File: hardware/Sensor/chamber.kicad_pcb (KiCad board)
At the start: 2 copper layers, 100 x 100 mm, 96 parts, among them J1 USB_B_Micro, J32 RF_Shield_Two_Pieces, J33 RF_Shield_Two_Pieces, J34 Conn_Coaxial, J51 Conn_02x05_Counter_Clockwise, J52 Conn_01x04, Q31 BC859, Q32 Q_NMOS_GDS, Q51 2N7002, Q52 Q_NPN_BEC, SW31 SW_DPDT_x2, SW32 SW_DPDT_x2, U31 MC34063AD, U32 LMC662, U33 LM358, U51 Opamp_Dual_Generic, U52 MCP3425A0T-ECH, U53 MCP3425A0T-ECH, U54 STM8S003F3P

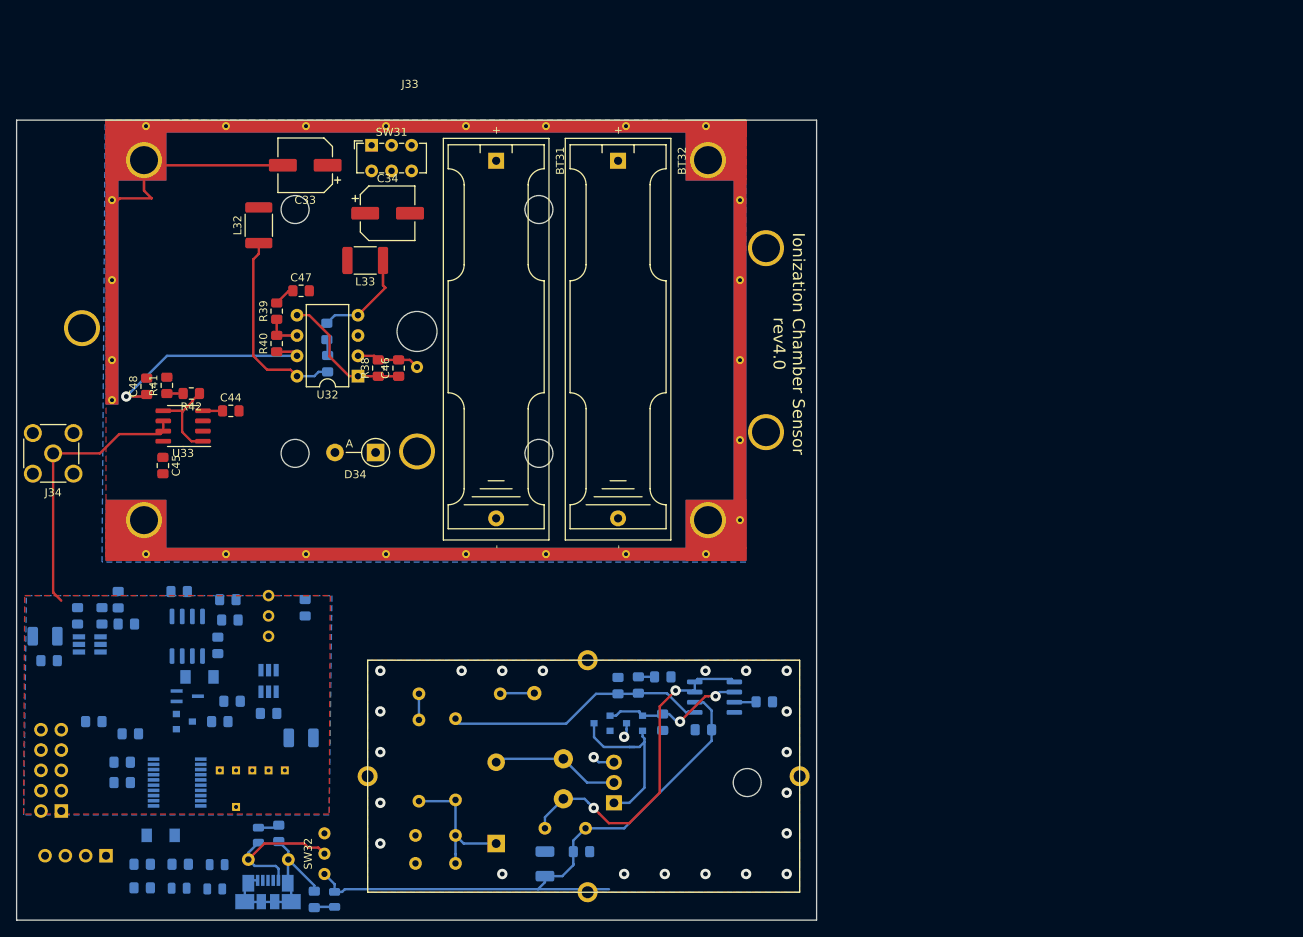
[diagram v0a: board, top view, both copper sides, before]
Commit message: ground between masses
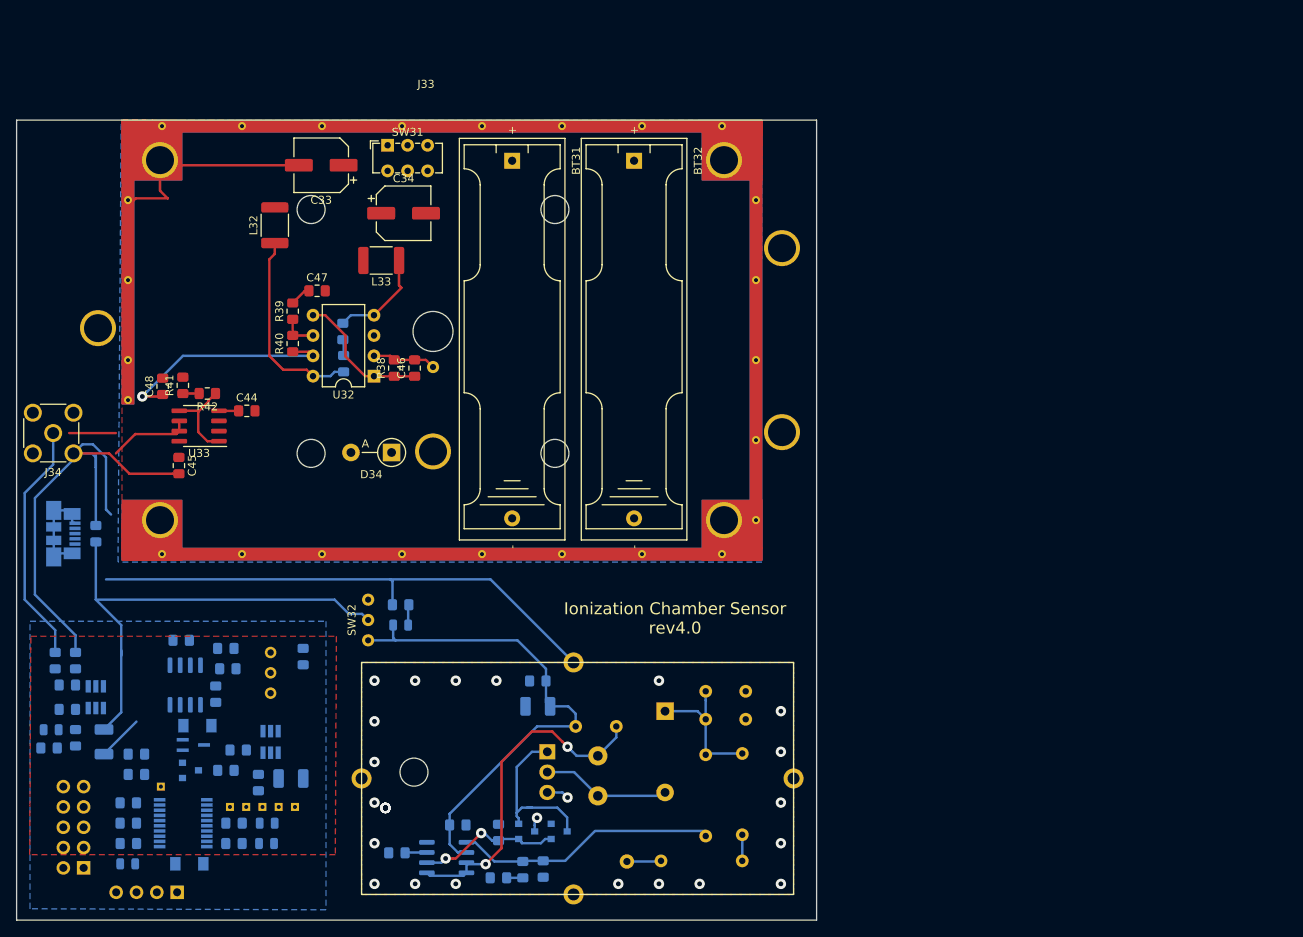
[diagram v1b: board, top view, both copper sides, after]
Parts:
- C1: footprint Capacitor_THT:C_Disc_D4.3mm_W1.9mm_P5.00mm -> Capacitor_SMD:C_0805_2012Metric_Pad1.15x1.40mm_HandSolder
- moved J32 61.8 mm to (95.4, 122.1), turned to 0 degrees
- moved J1 51.6 mm to (58.2, 106.0), turned to 90 degrees
- moved C32 49.7 mm to (99.9, 145.9), turned to 180 degrees
- moved C1 47.3 mm to (62.2, 106.1), turned to 270 degrees
- moved R36 42.9 mm to (143.0, 143.7), turned to 90 degrees
- moved U31 39.0 mm to (106.1, 146.5), turned to 0 degrees
- moved R43 38.4 mm to (100.3, 114.9), turned to 180 degrees
- moved C41 38.0 mm to (138.5, 125.8), turned to 0 degrees
- moved D31 35.3 mm to (100.3, 117.5), turned to 180 degrees
- moved C43 34.5 mm to (138.5, 129.3), turned to 0 degrees
- moved C31 32.9 mm to (107.5, 142.5), turned to 180 degrees
- moved R35 32.4 mm to (112.6, 149.1), turned to 180 degrees
- moved R33 31.8 mm to (138.5, 133.7), turned to 270 degrees
- moved R1 30.6 mm to (56.4, 132.8), turned to 0 degrees
- moved SW32 29.7 mm to (93.7, 116.8)
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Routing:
- net GND: track 57.9 -> 187.7 mm, vias 23 -> 28
- net VCC_5V: track 19.2 -> 61.4 mm
- net Net-(C2-Pad1): track 75.2 -> 62.4 mm
- net analog_output: track 35.0 -> 46.7 mm
- net Net-(D1-Pad1): track 2.67 -> 0.00 mm
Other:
- board text added: "400V DC chamber polarization"
- board text added: "Chamber signal amplifier"
- board text added: "DAC converter"

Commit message: befor board flip
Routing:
- net GND: track 187.7 -> 191.8 mm, vias 28 -> 20
- net Net-(C2-Pad1): track 62.4 -> 61.7 mm
- net Net-(C39-Pad1): track 32.5 -> 33.0 mm
- net analog_output: track 46.7 -> 46.1 mm

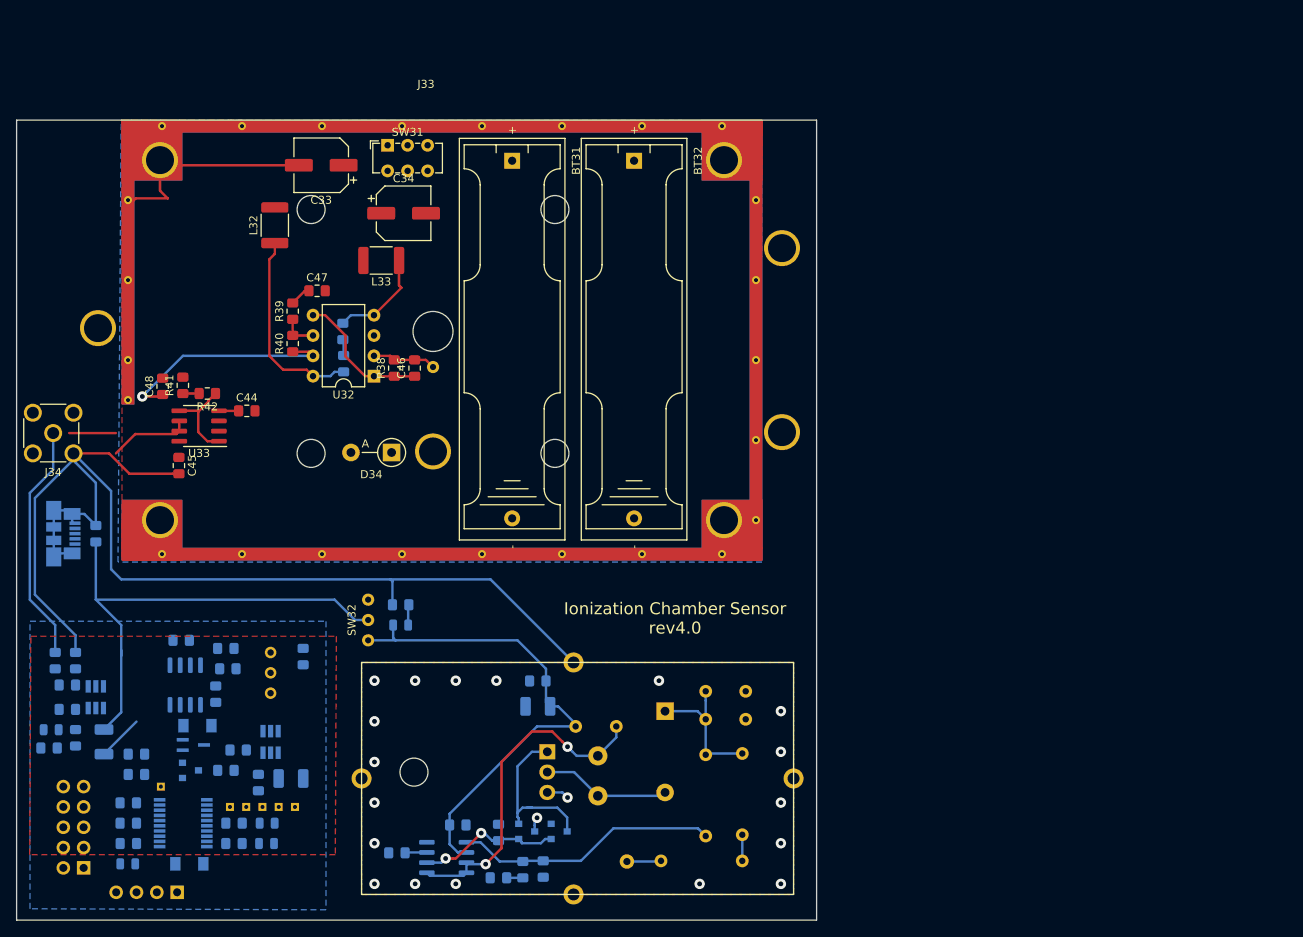
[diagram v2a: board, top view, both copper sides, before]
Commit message: dirty version of adc routing
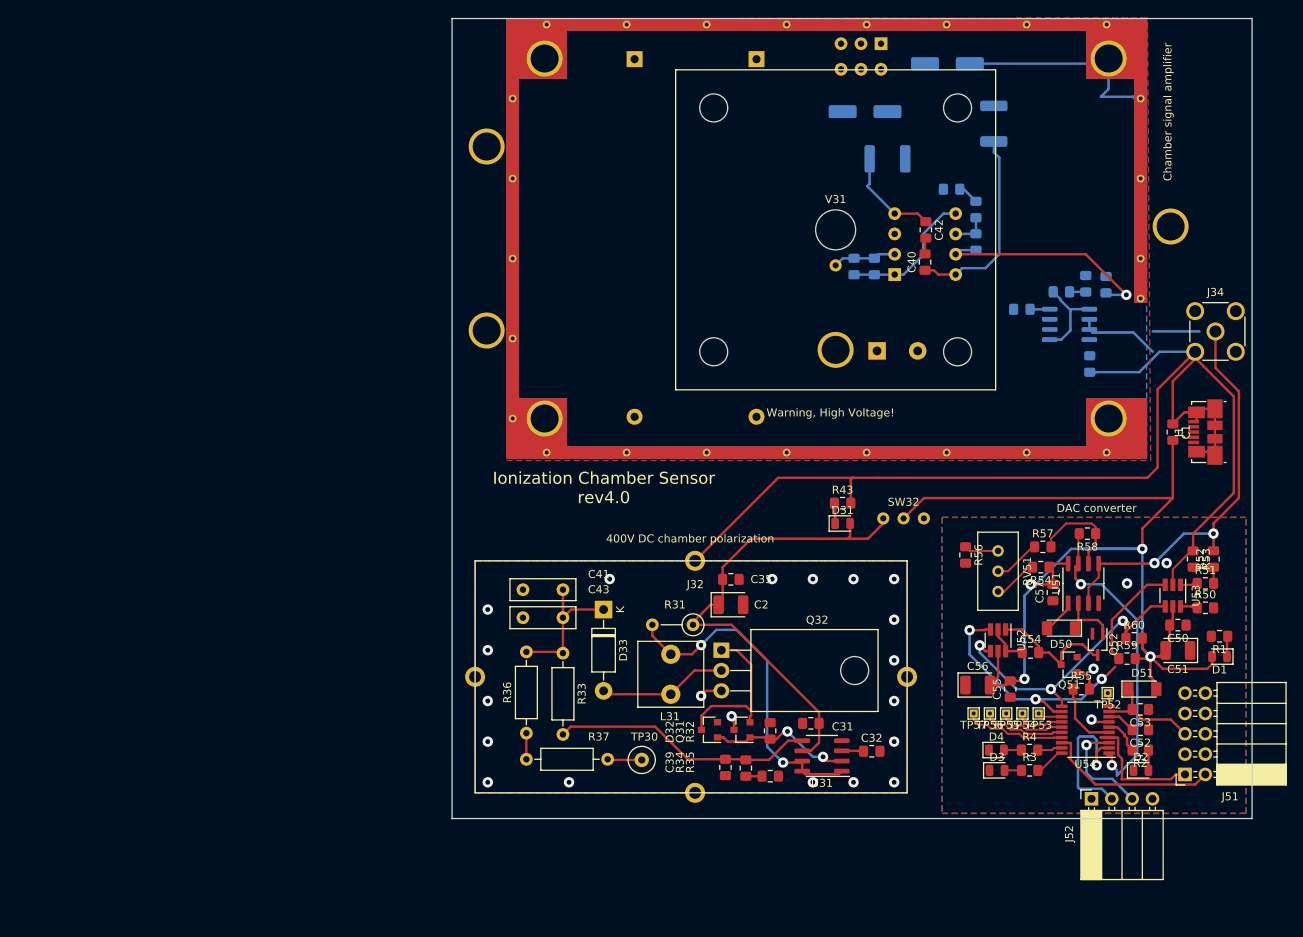
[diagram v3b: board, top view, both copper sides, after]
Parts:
- BT31, BT32, C33, C34, C44, C45, C46, C47, C48, D34, J33, L32, L33, R38, R39, R40, R41, R42, SW31, U32, U33: moved to B.Cu
- C1, C2, C31, C32, C35, C39, C40, C41, C42, C43, C50, C51, C52, C53, C54, C55, C56, C57, D1, D2, D3, D31, D32, D33, D4, D50, D51, J1, J32, J51, J52, L31, Q31, Q32, Q51, Q52, R1, R2, R3, R31, R32, R33, R34, R35, R36, R37, R4, R43, R50, R51, R52, R53, R54, R55, R56, R57, R58, R59, R60, RV51, TP30, TP52, TP53, TP54, TP55, TP56, TP57, U31, U51, U52, U53, U54, V31: moved to F.Cu
- moved R1 147.0 mm to (202.7, 118.9), turned to 180 degrees
- moved D1 146.3 mm to (202.7, 121.4), turned to 180 degrees
- moved J34 145.8 mm to (202.2, 80.8), turned to 270 degrees
- moved R52 145.3 mm to (201.9, 109.2)
- moved J1 143.3 mm to (200.9, 93.3)
- moved R50 142.8 mm to (200.9, 115.3), turned to 0 degrees
- moved R51 142.8 mm to (200.9, 112.3), turned to 0 degrees
- moved R53 140.3 mm to (199.4, 109.2)
- moved C50 138.5 mm to (197.5, 117.5), turned to 180 degrees
- moved J51 138.2 mm to (198.4, 136.1), turned to 180 degrees
- moved C1 135.2 mm to (196.8, 93.4)
- moved U53 135.2 mm to (196.8, 113.8)
- moved C51 134.7 mm to (197.5, 120.7), turned to 180 degrees
- moved J33 128.7 mm to (193.6, 41.7), turned to 180 degrees
- moved D2 127.2 mm to (192.9, 135.6), turned to 0 degrees
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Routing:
- net VCC_5V: track 61.4 -> 143.0 mm, vias 0 -> 4
- net /DataAcquisition/SCL: track 0.00 -> 45.9 mm, vias 0 -> 3
- net /DataAcquisition/INT0: track 0.00 -> 40.0 mm, vias 0 -> 2
- net /DataAcquisition/SDA: track 0.00 -> 38.0 mm, vias 0 -> 3
- net /DataAcquisition/SWIM: track 0.00 -> 22.1 mm
- net analog_output: track 46.1 -> 67.5 mm, vias 0 -> 2
- net /DataAcquisition/TX: track 0.00 -> 20.1 mm, vias 0 -> 1
- net /DataAcquisition/RST: track 0.00 -> 16.7 mm
- net Net-(C54-Pad2): track 0.00 -> 15.8 mm
- net /DataAcquisition/VCC_PROG: track 0.00 -> 13.6 mm
- net /DataAcquisition/RX: track 0.00 -> 13.5 mm, vias 0 -> 1
- net Net-(TP57-Pad1): track 0.00 -> 12.7 mm
- net Net-(R57-Pad2): track 0.00 -> 12.5 mm
- net Net-(TP56-Pad1): track 0.00 -> 10.6 mm
- net /DataAcquisition/RST_PEAK: track 0.00 -> 8.73 mm
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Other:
- net class Default: clearance 0.3048 -> 0.254
- rule trace_clearance: 0.3048 -> 0.254

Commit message: ruting amplifier part
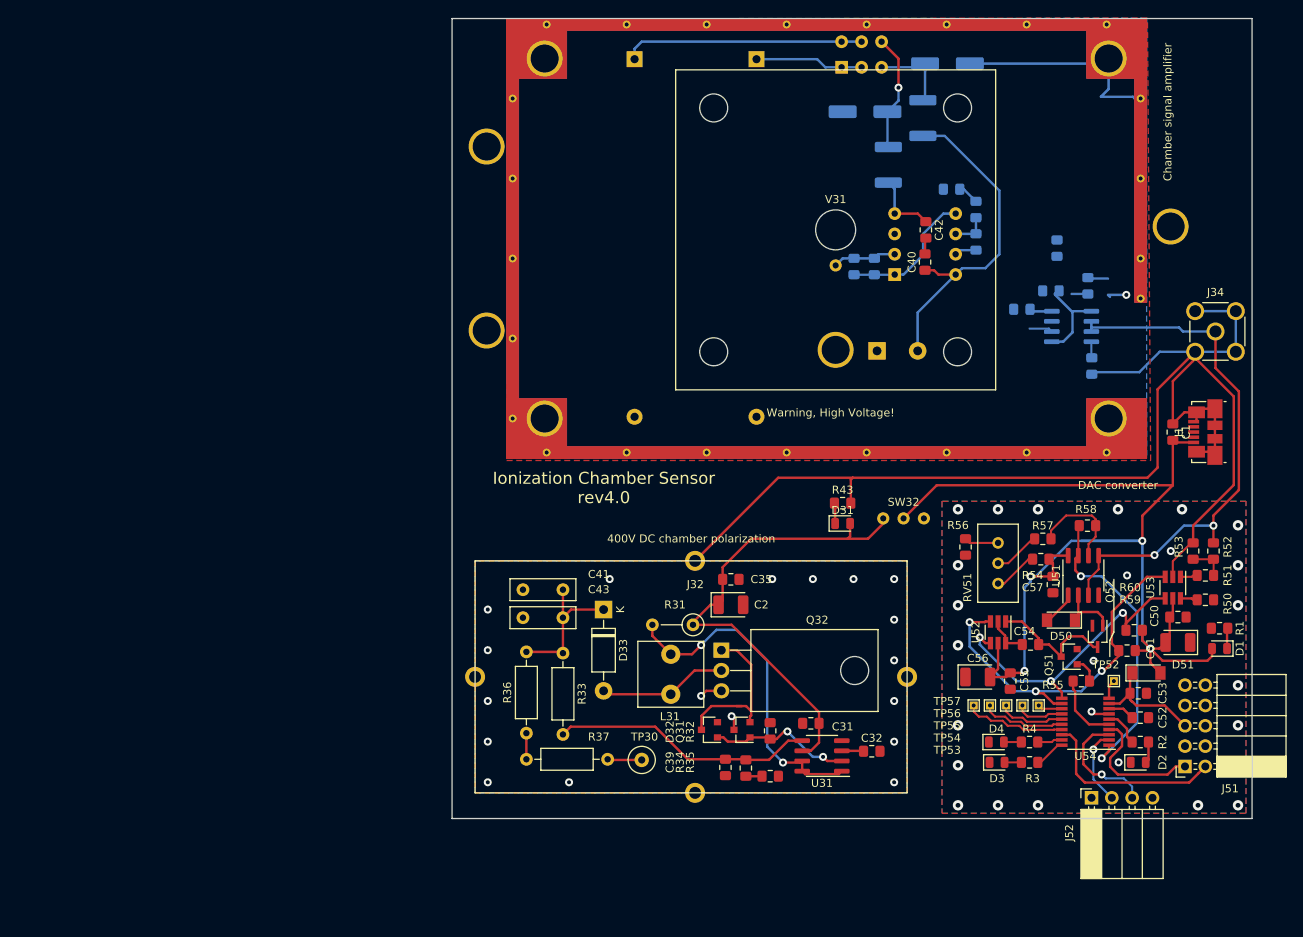
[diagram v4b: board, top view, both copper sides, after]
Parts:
- moved L32 8.90 mm to (165.6, 54.1)
- moved C48 7.65 mm to (182.4, 70.4)
- moved SW31 5.75 mm to (155.4, 47.8), turned to 0 degrees
- moved D51 2.08 mm to (193.5, 123.5)
- moved C53 2.03 mm to (192.5, 126.0)
- moved TP52 1.69 mm to (189.5, 124.5)
- moved C52 1.51 mm to (192.8, 129.0)
- moved R42 1.32 mm to (181.6, 75.7), turned to 180 degrees
- moved D2 1.05 mm to (192.5, 134.6)
- moved C50 1.00 mm to (197.5, 116.5)
- moved C51 1.00 mm to (197.5, 119.7)
- moved C54 1.00 mm to (179.1, 119.9)
- moved C55 1.00 mm to (176.5, 124.5)
- moved C56 1.00 mm to (172.5, 124.0)
- moved C57 1.00 mm to (181.9, 112.4)
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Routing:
- net Net-(BT32-Pad1): track 0.00 -> 30.0 mm
- net Net-(C48-Pad1): track 28.8 -> 5.39 mm
- net +BATT: track 24.9 -> 44.5 mm
- net Net-(C34-Pad1): track 0.00 -> 14.7 mm, vias 0 -> 1
- net Net-(BT31-Pad1): track 0.00 -> 13.6 mm
- net GND: track 199.1 -> 212.5 mm, vias 24 -> 44
- net Net-(C33-Pad1): track 0.00 -> 11.2 mm
- net /DataAcquisition/TX: track 20.1 -> 9.60 mm
- net -BATT: track 15.2 -> 11.5 mm
- net Net-(R41-Pad1): track 2.04 -> 4.99 mm
- net Net-(C48-Pad2): track 0.00 -> 2.57 mm
- net /DataAcquisition/INT0: track 40.0 -> 37.9 mm
- net /DataAcquisition/SWIM: track 22.1 -> 23.7 mm
- net VCC_5V: track 143.0 -> 144.6 mm
- net /DataAcquisition/RX: track 13.5 -> 14.9 mm
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
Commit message: befoure routing amp gnd
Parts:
- moved C48 6.36 mm to (176.0, 70.6), turned to 0 degrees
- moved R42 5.11 mm to (186.7, 76.2)
- moved R41 2.87 mm to (183.4, 75.4)
- moved C42 0.80 mm to (165.2, 67.8)
- moved C40 0.80 mm to (165.1, 71.8)
- moved C44 0.24 mm to (178.0, 78.2)
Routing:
- net +BATT: track 44.5 -> 82.9 mm, vias 0 -> 4
- net -BATT: track 11.5 -> 44.8 mm, vias 0 -> 2
- net Net-(C48-Pad2): track 2.57 -> 8.31 mm
- net Net-(D34-Pad1): track 0.00 -> 5.23 mm
- net Net-(R41-Pad1): track 4.99 -> 8.07 mm
- net Net-(R42-Pad1): track 11.3 -> 9.90 mm
- net Net-(C48-Pad1): track 5.39 -> 5.50 mm, vias 1 -> 0

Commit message: all done for raw version
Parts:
- moved C40 1.00 mm to (166.1, 71.9)
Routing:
- net GND: track 212.5 -> 470.3 mm, vias 44 -> 52
- net +BATT: track 82.9 -> 81.9 mm

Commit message: ready to sent to manufacture
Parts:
- added D35: red, LED_SMD:LED_0805_2012Metric, F.Cu at (148.9, 104.6)
- added R44: 520R, Resistor_SMD:R_0805_2012Metric_Pad1.15x1.40mm_HandSolder, F.Cu at (149.1, 102.1)
- added TP31: TestPoint, TestPoint:TestPoint_Loop_D2.60mm_Drill0.9mm_Beaded, F.Cu at (150.4, 83.1)
- moved D31 1.27 mm to (154.3, 104.8)
- moved R43 1.27 mm to (154.3, 102.2)
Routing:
- net GND: track 470.3 -> 484.6 mm, vias 52 -> 54
- net Net-(D34-Pad1): track 5.23 -> 9.57 mm
- net Net-(D35-Pad1): track 0.00 -> 2.58 mm
- net Net-(C2-Pad1): track 60.9 -> 62.5 mm
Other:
- board text added: "ADC converter"
- board text added: "HV power on/off"
- board text added: "HV+ADC power"
- board text added: "analog output"
- board text added: "power on"
- board text removed: "DAC converter"
